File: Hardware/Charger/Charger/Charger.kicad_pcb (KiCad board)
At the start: 2 copper layers, 89 parts, among them J201 Conn_01x02, J301 Conn_01x04_Socket, J302 Conn_02x03_Counter_Clockwise, J401 USB_C_Receptacle_USB2.0_16P, SW301 SW_Push, SW302 SW_Push, U301 TCAN1042VDRQ1, U302 STM32G473CCTx, U303 MAX7221xWG, U304 LTV-356T, U305 CC56-12SEKWA, U306 MCP41U83x-xxxx-ST, U307 MCP41U83x-xxxx-ST, U308 MCP41U83x-xxxx-ST, U309 MCP41U83x-xxxx-ST, U401 USBLC6-2SC6, Y301 48 MHz

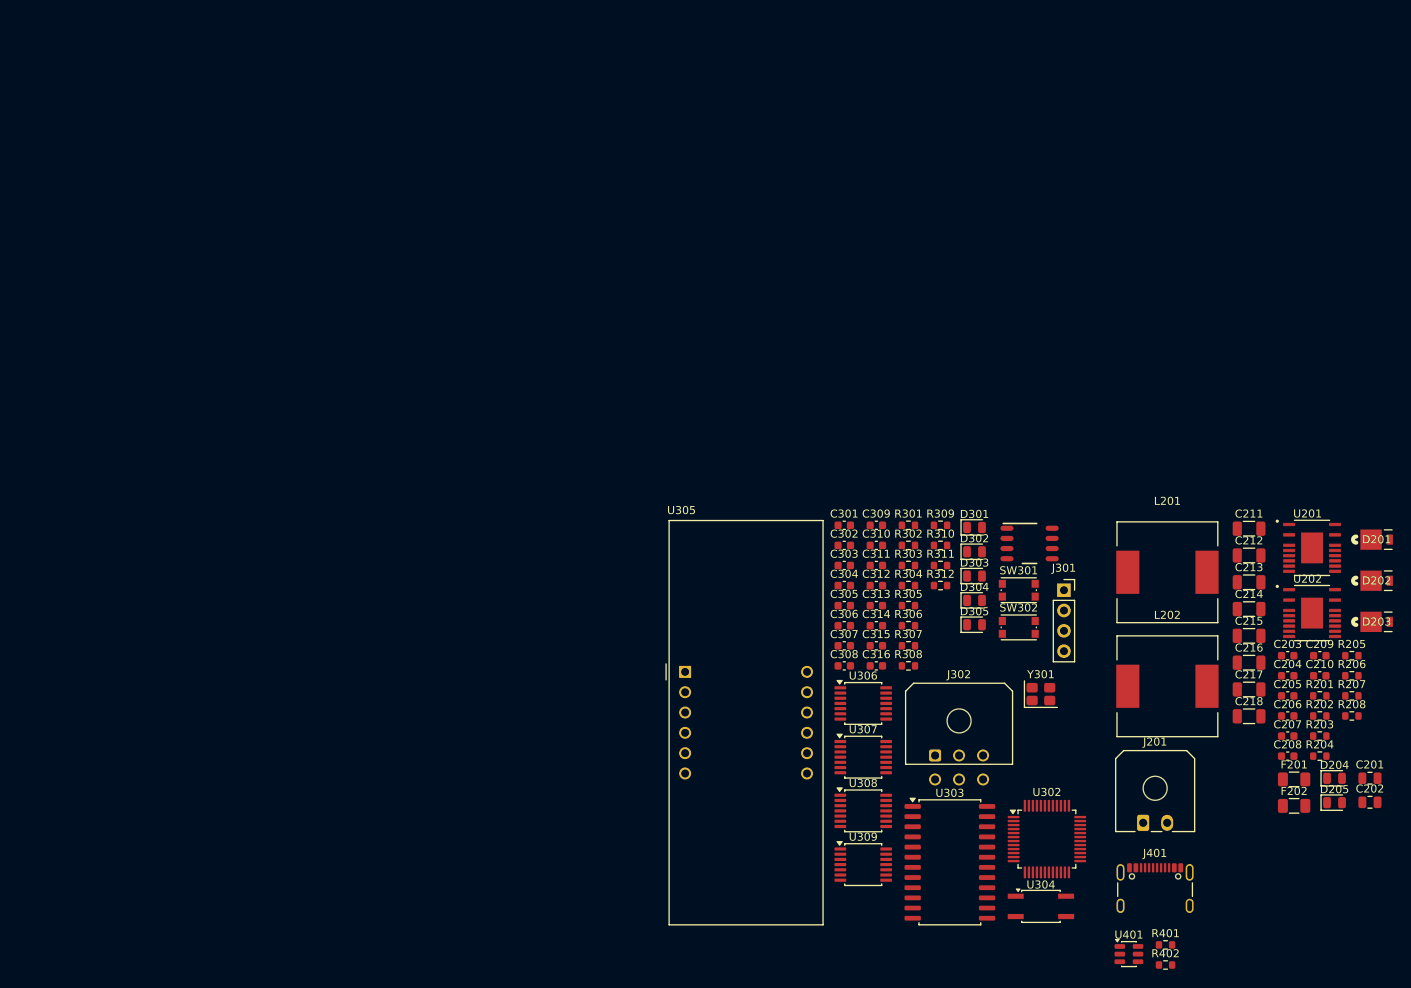
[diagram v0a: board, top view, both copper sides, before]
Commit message: Completed PCB layout of charger
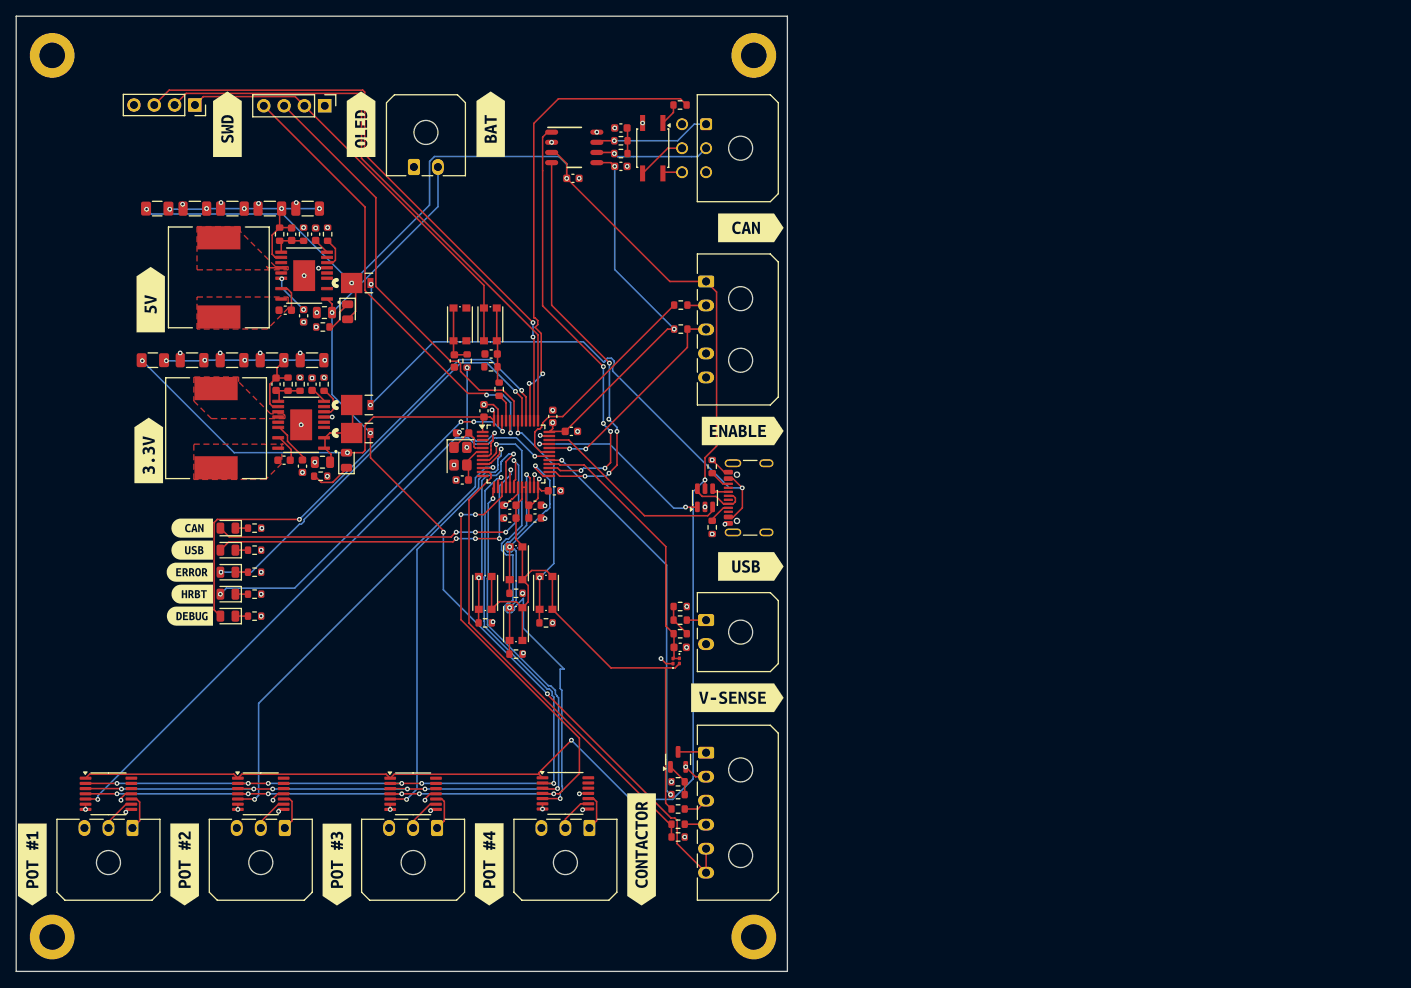
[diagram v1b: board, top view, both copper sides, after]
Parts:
- removed C316: 1uF, Capacitor_SMD:C_0603_1608Metric
- removed R306: 9.53k, Resistor_SMD:R_0603_1608Metric
- removed U303: MAX7221xWG, Package_SO:SOIC-24W_7.5x15.4mm_P1.27mm
- removed U305: CC56-12SEKWA, Display_7Segment:CA56-12SEKWA
- removed U306, U307, U308, U309: MCP41U83x-xxxx-ST, Package_SO:TSSOP-14_4.4x5mm_P0.65mm
- added C1: 100nF, Capacitor_SMD:C_0603_1608Metric, F.Cu at (121.0, 109.4)
- added D1: D_Schottky, Diode_SMD:D_0201_0603Metric, F.Cu at (120.9, 111.1)
- added D2: D_Schottky, Diode_SMD:D_0201_0603Metric, F.Cu at (120.1, 111.1)
- added J1: Conn_01x06, Connector_Molex:Molex_Micro-Fit_3.0_43650-0600_1x06_P3.00mm_Horizontal, F.Cu at (124.2, 122.6)
- added J10: Conn_01x03, Connector_Molex:Molex_Micro-Fit_3.0_43650-0300_1x03_P3.00mm_Horizontal, F.Cu at (90.6, 132.0)
- added J11: Conn_01x03, Connector_Molex:Molex_Micro-Fit_3.0_43650-0300_1x03_P3.00mm_Horizontal, F.Cu at (71.6, 132.0)
- added J12: Conn_01x03, Connector_Molex:Molex_Micro-Fit_3.0_43650-0300_1x03_P3.00mm_Horizontal, F.Cu at (52.5, 132.0)
- added J2: Conn_01x02, Connector_Molex:Molex_Micro-Fit_3.0_43650-0200_1x02_P3.00mm_Horizontal, F.Cu at (124.2, 106.0)
- added J3: Conn_01x05, Connector_Molex:Molex_Micro-Fit_3.0_43650-0500_1x05_P3.00mm_Horizontal, F.Cu at (124.2, 63.7)
- added J6: Conn_01x04, Connector_PinHeader_2.54mm:PinHeader_1x04_P2.54mm_Vertical, F.Cu at (76.6, 41.7)
- added J9: Conn_01x03, Connector_Molex:Molex_Micro-Fit_3.0_43650-0300_1x03_P3.00mm_Horizontal, F.Cu at (109.7, 132.0)
- added Q401: DMN10H220L, Package_TO_SOT_SMD:SOT-23, F.Cu at (120.7, 123.4)
- added R1: 100k, Resistor_SMD:R_0603_1608Metric, F.Cu at (120.7, 129.6)
- added R10: 330, Resistor_SMD:R_0603_1608Metric, F.Cu at (121.1, 66.6)
- added R2: 100k, Resistor_SMD:R_0603_1608Metric, F.Cu at (120.7, 126.2)
- added R28: 10k, Resistor_SMD:R_0603_1608Metric, F.Cu at (100.5, 102.6)
- added R29: 10k, Resistor_SMD:R_0603_1608Metric, F.Cu at (100.5, 110.2)
- added R3: 10k, Resistor_SMD:R_0603_1608Metric, F.Cu at (120.7, 127.8)
- added R32: 10k, Resistor_SMD:R_0603_1608Metric, F.Cu at (104.2, 106.3)
- added R33: 10k, Resistor_SMD:R_0603_1608Metric, F.Cu at (96.6, 106.3)
- added R4: 100k, Resistor_SMD:R_0603_1608Metric, F.Cu at (120.7, 131.5)
- added R5: 100k, Resistor_SMD:R_0603_1608Metric, F.Cu at (120.7, 133.1)
- added R6: 200k, Resistor_SMD:R_0603_1608Metric, F.Cu at (121.0, 106.0)
- added R7: 10k, Resistor_SMD:R_0603_1608Metric, F.Cu at (121.0, 104.3)
- added R8: 1k, Resistor_SMD:R_0603_1608Metric, F.Cu at (121.0, 107.7)
- added R9: 10k, Resistor_SMD:R_0603_1608Metric, F.Cu at (121.1, 69.6)
- added REF**: MountingHole_3.2mm_M3_DIN965_Pad, MountingHole:MountingHole_3.2mm_M3_DIN965_Pad, F.Cu at (42.5, 35.4)
- added REF**: MountingHole_3.2mm_M3_DIN965_Pad, MountingHole:MountingHole_3.2mm_M3_DIN965_Pad, F.Cu at (42.5, 145.6)
- added REF**: MountingHole_3.2mm_M3_DIN965_Pad, MountingHole:MountingHole_3.2mm_M3_DIN965_Pad, F.Cu at (130.2, 145.6)
- added REF**: MountingHole_3.2mm_M3_DIN965_Pad, MountingHole:MountingHole_3.2mm_M3_DIN965_Pad, F.Cu at (130.2, 35.4)
- added SW3: SW_Push, Button_Switch_SMD:SW_Push_1P1T_NO_CK_KMR2, F.Cu at (100.5, 98.9)
- added SW4: SW_Push, Button_Switch_SMD:SW_Push_1P1T_NO_CK_KMR2, F.Cu at (100.5, 106.5)
- added SW5: SW_Push, Button_Switch_SMD:SW_Push_1P1T_NO_CK_KMR2, F.Cu at (104.2, 102.6)
- added SW6: SW_Push, Button_Switch_SMD:SW_Push_1P1T_NO_CK_KMR2, F.Cu at (96.6, 102.6)
- added U10: MCP41U83x-xxxx-ST, Package_SO:TSSOP-14_4.4x5mm_P0.65mm, F.Cu at (49.5, 127.7)
- added U7: MCP41U83x-xxxx-ST, Package_SO:TSSOP-14_4.4x5mm_P0.65mm, F.Cu at (106.7, 127.6)
- added U8: MCP41U83x-xxxx-ST, Package_SO:TSSOP-14_4.4x5mm_P0.65mm, F.Cu at (87.6, 127.7)
- added U9: MCP41U83x-xxxx-ST, Package_SO:TSSOP-14_4.4x5mm_P0.65mm, F.Cu at (68.6, 127.7)
- added kibuzzard-69B34D34: G***, kibuzzard-69B34D34, F.Cu at (54.8, 65.9)
- added kibuzzard-69B34D41: G***, kibuzzard-69B34D41, F.Cu at (54.6, 84.8)
- added kibuzzard-69B34D81: G***, kibuzzard-69B34D81, F.Cu at (81.1, 44.0)
- added kibuzzard-69B34DA5: G***, kibuzzard-69B34DA5, F.Cu at (40.0, 136.5)
- added kibuzzard-69B34DB2: G***, kibuzzard-69B34DB2, F.Cu at (59.1, 136.5)
- added kibuzzard-69B34DBF: G***, kibuzzard-69B34DBF, F.Cu at (78.1, 136.6)
- added kibuzzard-69B34DC8: G***, kibuzzard-69B34DC8, F.Cu at (97.1, 136.5)
- added kibuzzard-69B34E29: G***, kibuzzard-69B34E29, F.Cu at (116.2, 134.7)
- added kibuzzard-69B34E60: G***, kibuzzard-69B34E60, F.Cu at (128.1, 115.7)
- added kibuzzard-69B34E6D: G***, kibuzzard-69B34E6D, F.Cu at (129.8, 99.3)
- added kibuzzard-69B34E8A: G***, kibuzzard-69B34E8A, F.Cu at (128.8, 82.3)
- added kibuzzard-69B34E97: G***, kibuzzard-69B34E97, F.Cu at (129.8, 57.0)
- added kibuzzard-69B34ED3: G***, kibuzzard-69B34ED3, F.Cu at (97.3, 44.0)
- added kibuzzard-69B34F21: G***, kibuzzard-69B34F21, F.Cu at (64.4, 44.0)
- added kibuzzard-69B36C6C: G***, kibuzzard-69B36C6C, F.Cu at (60.0, 94.5)
- added kibuzzard-69B36C7B: G***, kibuzzard-69B36C7B, F.Cu at (60.0, 97.2)
- added kibuzzard-69B36C96: G***, kibuzzard-69B36C96, F.Cu at (59.7, 100.0)
- added kibuzzard-69B36CA5: G***, kibuzzard-69B36CA5, F.Cu at (60.0, 102.7)
- added kibuzzard-69B36CC2: G***, kibuzzard-69B36CC2, F.Cu at (59.7, 105.5)
- moved F1 159.0 mm to (55.6, 54.5)
- moved F2 153.1 mm to (55.1, 73.5), turned to 180 degrees
- moved C18 144.8 mm to (60.3, 54.5), turned to 180 degrees
- moved R13 144.4 mm to (70.9, 57.8), turned to -90 degrees
- moved C2 143.1 mm to (76.5, 67.5), turned to 180 degrees
- moved R14 142.8 mm to (73.9, 57.8), turned to 90 degrees
- moved C19 139.4 mm to (60.0, 73.5), turned to 180 degrees
- moved C8 139.4 mm to (72.4, 57.8), turned to -90 degrees
- moved C16 137.8 mm to (65.0, 54.5), turned to 180 degrees
- moved D7 137.8 mm to (79.4, 67.5), turned to -90 degrees
- moved C3 137.7 mm to (76.3, 86.2), turned to 180 degrees
- moved R18 137.5 mm to (76.3, 69.3)
- moved R15 137.2 mm to (72.0, 76.5), turned to -90 degrees
- moved R11 136.8 mm to (76.9, 57.8), turned to 90 degrees
- moved R16 136.4 mm to (73.5, 76.5), turned to 90 degrees
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- renumbered C209 to C10, C210 to C11, C211 to C12, C212 to C13, C213 to C14, C214 to C15, C215 to C16, C216 to C17, C217 to C18, C218 to C19, C201 to C2, C301 to C20, C302 to C21, C303 to C22, C304 to C23, C305 to C24, C306 to C25, C307 to C26, C308 to C27, C309 to C28, C310 to C29, C202 to C3, C311 to C30, C312 to C31, C313 to C32, C314 to C33, C315 to C34, C203 to C4, C204 to C5, C205 to C6, C206 to C7, C207 to C8, C208 to C9, D303 to D10, D304 to D11, D305 to D12, D201 to D3, D202 to D4, D203 to D5, D204 to D6, D205 to D7, D301 to D8, D302 to D9, F201 to F1, F202 to F2, J201 to J4, J301 to J5, J302 to J7, J401 to J8, L201 to L1, L202 to L2, R201 to R11, R202 to R12, R203 to R13, R204 to R14, R205 to R15, R206 to R16, R207 to R17, R208 to R18, R301 to R19, R302 to R20, R303 to R21, R304 to R22, R305 to R23, R307 to R24, R308 to R25, R309 to R26, R310 to R27, R311 to R30, R312 to R31, R401 to R34, R402 to R35, SW301 to SW1, SW302 to SW2, U201 to U1, U202 to U2, U301 to U3, U302 to U4, U304 to U5, U401 to U6, Y301 to Y1
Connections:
- net +12V renamed +24V
- U4 pad 10: unconnected-(U302-PA2-Pad10) -> /DigiPot/~{CS}3
- U4 pad 11: unconnected-(U302-PA3-Pad11) -> /A_SENSE
- U4 pad 16: unconnected-(U302-PB0-Pad16) -> /stm32/BACK
- U4 pad 22: unconnected-(U302-PB10-Pad22) -> /stm32/UP
- U4 pad 25: unconnected-(U302-PB11-Pad25) -> /stm32/DOWN
- U4 pad 28: unconnected-(U302-PB14-Pad28) -> /VSENSE1
- U4 pad 29: unconnected-(U302-PB15-Pad29) -> /CONTACTOR_CTRL
- U4 pad 30: unconnected-(U302-PA8-Pad30) -> /DigiPot/~{CS}4
- U4 pad 31: /stm32/DISP_~{CS} -> /DIN
- U4 pad 32: unconnected-(U302-PA10-Pad32) -> /NO
- U4 pad 39: unconnected-(U302-PA15-Pad39) -> /stm32/CTRL_NONCRIT_CHECK
- U4 pad 42: unconnected-(U302-PB5-Pad42) -> /stm32/SELECT
- U4 pad 43: unconnected-(U302-PB6-Pad43) -> /stm32/SCL
- U4 pad 44: unconnected-(U302-PB7-Pad44) -> /stm32/SDA
- U4 pad 8: unconnected-(U302-PA0-Pad8) -> /DigiPot/~{CS}1
- U4 pad 9: unconnected-(U302-PA1-Pad9) -> /DigiPot/~{CS}2
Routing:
- net +3.3V: track 0.00 -> 258.3 mm, vias 0 -> 7
- net +5V: track 0.00 -> 249.2 mm, vias 0 -> 5
- net +24V: track 0.00 -> 118.3 mm, vias 0 -> 4
- net /stm32/SPI1_MOSI: track 0.00 -> 112.7 mm, vias 0 -> 8
- net /stm32/SPI1_SCK: track 0.00 -> 107.3 mm, vias 0 -> 7
- net /stm32/SPI1_MISO: track 0.00 -> 107.2 mm, vias 0 -> 7
- net /Power Supplies/5v_USBC: track 0.00 -> 81.0 mm, vias 0 -> 3
- net /DigiPot/~{CS}4: track 0.00 -> 78.6 mm, vias 0 -> 2
- net /stm32/SWCLK: track 0.00 -> 77.0 mm, vias 0 -> 2
- net /stm32/SWDIO: track 0.00 -> 74.0 mm
- net /stm32/DEBUG1: track 0.00 -> 64.5 mm, vias 0 -> 2
- net /DigiPot/~{CS}1: track 0.00 -> 62.9 mm, vias 0 -> 2
- net /stm32/CTRL_NONCRIT_CHECK: track 0.00 -> 59.7 mm, vias 0 -> 2
- net /A_SENSE: track 0.00 -> 58.2 mm
- net /DigiPot/~{CS}3: track 0.00 -> 57.8 mm, vias 0 -> 2
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- added copper zone on In1.Cu, net GND
- added copper zone on F.Cu, net Net-(U1-IND)
- added copper zone on F.Cu, net Net-(U1-SW)
- added copper zone on F.Cu, net Net-(U2-IND)
- added copper zone on F.Cu, net Net-(U2-SW)
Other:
- board outline added: 96.4 x 119.4 mm
- copper layers 2 -> 4

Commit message: edits to charger and made ground ring bodge board. Both ready for PCB fab
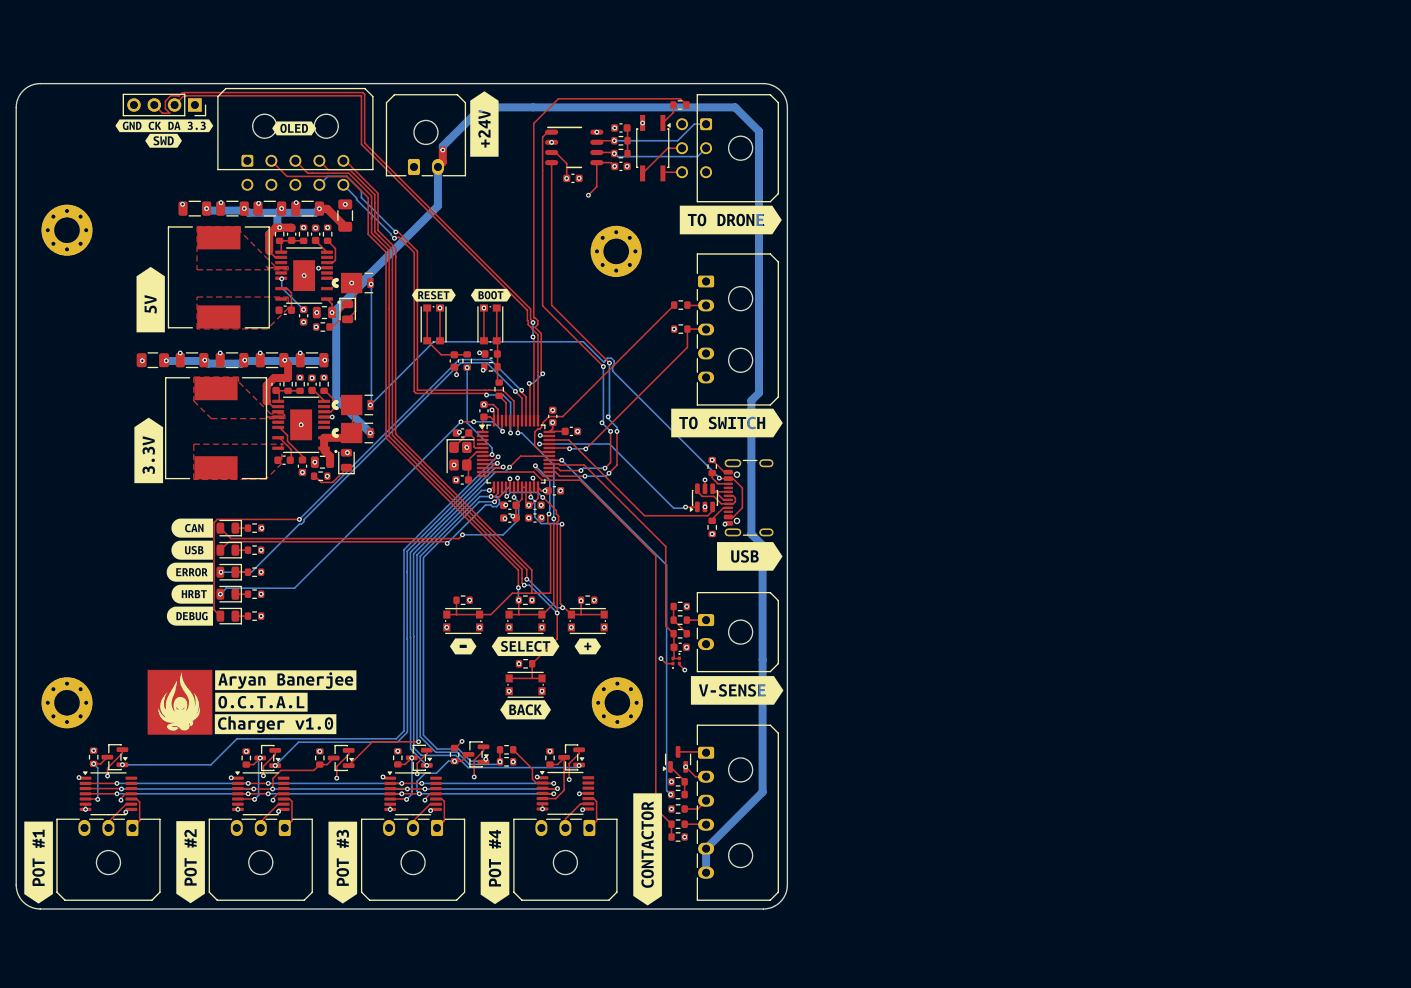
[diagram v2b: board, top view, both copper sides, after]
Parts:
- removed J6: Conn_01x04, Connector_PinHeader_2.54mm:PinHeader_1x04_P2.54mm_Vertical
- removed REF** (x4): MountingHole_3.2mm_M3_DIN965_Pad, MountingHole:MountingHole_3.2mm_M3_DIN965_Pad
- removed kibuzzard-69B34D81: G***, kibuzzard-69B34D81
- removed kibuzzard-69B34E8A: G***, kibuzzard-69B34E8A
- removed kibuzzard-69B34E97: G***, kibuzzard-69B34E97
- removed kibuzzard-69B34ED3: G***, kibuzzard-69B34ED3
- removed kibuzzard-69B34F21: G***, kibuzzard-69B34F21
- added G*** (x2): LOGO, LOGO, F.Cu at (58.5, 116.2)
- added H301: MountingHole_Pad, MountingHole:MountingHole_3.2mm_M3_Pad_Via, F.Cu at (44.4, 57.2)
- added H302: MountingHole_Pad, MountingHole:MountingHole_3.2mm_M3_Pad_Via, F.Cu at (113.0, 59.9)
- added H303: MountingHole_Pad, MountingHole:MountingHole_3.2mm_M3_Pad_Via, F.Cu at (44.4, 116.3)
- added H304: MountingHole_Pad, MountingHole:MountingHole_3.2mm_M3_Pad_Via, F.Cu at (113.2, 116.3)
- added J301: Conn_02x05_Counter_Clockwise, Connector_Molex:Molex_Micro-Fit_3.0_43045-1000_2x05_P3.00mm_Horizontal, F.Cu at (66.9, 48.6)
- added Q501: DMN10H220L, Package_TO_SOT_SMD:SOT-23, F.Cu at (107.4, 123.2)
- added Q502: DMN10H220L, Package_TO_SOT_SMD:SOT-23, F.Cu at (95.5, 122.8)
- added Q503: DMN10H220L, Package_TO_SOT_SMD:SOT-23, F.Cu at (88.4, 123.2)
- added Q504: DMN10H220L, Package_TO_SOT_SMD:SOT-23, F.Cu at (69.4, 123.2)
- added Q505: DMN10H220L, Package_TO_SOT_SMD:SOT-23, F.Cu at (50.3, 123.1)
- added Q506: DMN10H220L, Package_TO_SOT_SMD:SOT-23, F.Cu at (78.6, 123.2)
- added R301: 1k, Resistor_SMD:R_0603_1608Metric, F.Cu at (99.3, 122.2)
- added R302: 2.2k, Resistor_SMD:R_0603_1608Metric, F.Cu at (99.3, 123.7)
- added R501: 1k, Resistor_SMD:R_0603_1608Metric, F.Cu at (104.7, 123.2)
- added R502: 1k, Resistor_SMD:R_0603_1608Metric, F.Cu at (92.8, 122.8)
- added R503: 1k, Resistor_SMD:R_0603_1608Metric, F.Cu at (85.7, 123.2)
- added R504: 1k, Resistor_SMD:R_0603_1608Metric, F.Cu at (66.8, 123.2)
- added R505: 1k, Resistor_SMD:R_0603_1608Metric, F.Cu at (47.7, 123.1)
- added R506: 1k, Resistor_SMD:R_0603_1608Metric, F.Cu at (76.0, 123.2)
- added kibuzzard-690FB638: G***, kibuzzard-690FB638, F.Cu at (56.4, 46.1)
- added kibuzzard-690FB70C: G***, kibuzzard-690FB70C, F.Cu at (56.5, 44.2)
- added kibuzzard-69B81BEB: G***, kibuzzard-69B81BEB, F.Cu at (127.3, 56.0)
- added kibuzzard-69B81C0B: G***, kibuzzard-69B81C0B, F.Cu at (126.8, 81.3)
- added kibuzzard-69B81D82: G***, kibuzzard-69B81D82, F.Cu at (68.7, 116.2)
- added kibuzzard-69B81DBD: G***, kibuzzard-69B81DBD, F.Cu at (70.4, 119.0)
- added kibuzzard-69B81DEB: G***, kibuzzard-69B81DEB, F.Cu at (71.7, 113.5)
- added kibuzzard-69B81E61: G***, kibuzzard-69B81E61, F.Cu at (90.2, 65.4)
- added kibuzzard-69B81E77: G***, kibuzzard-69B81E77, F.Cu at (97.3, 65.4)
- added kibuzzard-69B821F4: G***, kibuzzard-69B821F4, F.Cu at (93.9, 109.3)
- added kibuzzard-69B82222: G***, kibuzzard-69B82222, F.Cu at (109.5, 109.3)
- added kibuzzard-69B82233: G***, kibuzzard-69B82233, F.Cu at (101.7, 109.3)
- added kibuzzard-69B82281: G***, kibuzzard-69B82281, F.Cu at (101.7, 117.2)
- added kibuzzard-69B8247B: G***, kibuzzard-69B8247B, F.Cu at (72.8, 44.5)
- added kibuzzard-69B824A2: G***, kibuzzard-69B824A2, F.Cu at (96.5, 44.0)
- moved F1 23.5 mm to (79.1, 55.4), turned to -90 degrees
- moved SW6 12.5 mm to (101.7, 114.1), turned to 180 degrees
- moved R29 11.2 mm to (109.4, 103.5)
- moved SW3 9.78 mm to (93.9, 106.1), turned to 180 degrees
- moved SW4 8.98 mm to (109.5, 106.1), turned to 180 degrees
- moved R33 7.19 mm to (101.7, 111.5), turned to 180 degrees
- moved R28 6.67 mm to (93.9, 103.5)
- moved SW5 4.35 mm to (101.7, 106.1), turned to 180 degrees
- moved R32 3.83 mm to (101.7, 103.5)
- moved SW2 3.29 mm to (90.2, 69.0)
- moved kibuzzard-69B34E6D 1.27 mm to (129.7, 98.0)
- moved kibuzzard-69B34E60 0.92 mm to (128.1, 114.8)
- moved kibuzzard-69B34DA5 0.82 mm to (40.8, 136.3)
- moved kibuzzard-69B34DB2 0.80 mm to (59.8, 136.2)
- moved kibuzzard-69B34DBF 0.77 mm to (78.8, 136.3)
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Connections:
- R1 pad 1: +3.3V -> +3V3
- U10 pad 2: /stm32/SPI1_MISO -> /DigiPot/MISO
- U10 pad 3: /stm32/SPI1_SCK -> /DigiPot/SCK_L
- U10 pad 4: /stm32/SPI1_MOSI -> /DigiPot/MOSI_L
- U10 pad 5: /DigiPot/~{CS}4 -> /DigiPot/C4
- U4 pad 10: /DigiPot/~{CS}3 -> /DigiPot/~{CS}2
- U4 pad 14: /stm32/SPI1_MISO -> /stm32/SPI1_MISO_L
- U4 pad 30: /DigiPot/~{CS}4 -> /DigiPot/~{CS}1
- U4 pad 8: /DigiPot/~{CS}1 -> /DigiPot/~{CS}4
- U4 pad 9: /DigiPot/~{CS}2 -> /DigiPot/~{CS}3
- U7 pad 2: /stm32/SPI1_MISO -> /DigiPot/MISO
- U7 pad 3: /stm32/SPI1_SCK -> /DigiPot/SCK_L
- U7 pad 4: /stm32/SPI1_MOSI -> /DigiPot/MOSI_L
- U7 pad 5: /DigiPot/~{CS}1 -> /DigiPot/C1
- U8 pad 2: /stm32/SPI1_MISO -> /DigiPot/MISO
- U8 pad 3: /stm32/SPI1_SCK -> /DigiPot/SCK_L
- U8 pad 4: /stm32/SPI1_MOSI -> /DigiPot/MOSI_L
- U8 pad 5: /DigiPot/~{CS}2 -> /DigiPot/C2
- U9 pad 2: /stm32/SPI1_MISO -> /DigiPot/MISO
- U9 pad 3: /stm32/SPI1_SCK -> /DigiPot/SCK_L
- U9 pad 4: /stm32/SPI1_MOSI -> /DigiPot/MOSI_L
- U9 pad 5: /DigiPot/~{CS}3 -> /DigiPot/C3
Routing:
- net +3.3V: track 258.3 -> 32.2 mm, vias 7 -> 21
- net +5V: track 249.2 -> 34.4 mm, vias 5 -> 14
- net /stm32/SPI1_MISO: track 107.2 -> 0.00 mm, vias 7 -> 0
- net /stm32/BACK: track 28.7 -> 108.8 mm, vias 2 -> 4
- net /stm32/DOWN: track 21.3 -> 99.2 mm
- net /stm32/SELECT: track 28.3 -> 105.0 mm, vias 2 -> 4
- net /DigiPot/SCK_L: track 0.00 -> 75.6 mm, vias 0 -> 6
- net /DigiPot/MOSI_L: track 0.00 -> 72.2 mm, vias 0 -> 7
- net /DigiPot/MISO: track 0.00 -> 68.8 mm, vias 0 -> 6
- net /stm32/UP: track 27.5 -> 96.2 mm, vias 2 -> 5
- net /stm32/SPI1_MOSI: track 112.7 -> 45.9 mm, vias 8 -> 2
- net +24V: track 118.3 -> 185.0 mm, vias 4 -> 3
- net /stm32/SPI1_SCK: track 107.3 -> 46.6 mm, vias 7 -> 2
- net /stm32/SPI1_MISO_L: track 0.00 -> 49.3 mm, vias 0 -> 2
- net /stm32/SDA: track 57.7 -> 48.0 mm, vias 2 -> 3
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- added copper zone on In2.Cu, net +3.3V
- added copper zone on In2.Cu, net +5V
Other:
- board size 96.4 x 119.4 mm -> 96.4 x 103.2 mm
